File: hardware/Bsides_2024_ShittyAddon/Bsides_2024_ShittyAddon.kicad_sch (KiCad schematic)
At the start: 13 parts, among them J1 SWD, U1 PY32F002AA15M6TU

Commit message: feat(Hw): Update PCB
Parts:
- removed D4: Orange, LED_SMD:LED_0805_2012Metric, symbol Device:LED_Small
- removed R4: 330R, Resistor_SMD:R_0805_2012Metric, symbol Device:R_Small

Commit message: feat(Hw): Update PCB
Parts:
- removed J1: SWD, Footprints:PinHeader_1x04_P2.54mm_Vertical, symbol Connector:Conn_01x04_Pin
- added J2: Conn_02x03_Odd_Even, Footprints:B-2100N06P-B111_CKM, symbol Connector_Generic:Conn_02x03_Odd_Even
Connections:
- net +3.3V: now also J2.6 (Pin_6)
- net GND: now also J2.5 (Pin_5)
- net SWCLK: now also J2.2 (Pin_2)
- net SWDIO: now also J2.1 (Pin_1)
- no-connect marks 0 -> 2
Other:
- note added: "Shitty Add-on"

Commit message: Update route and schematic
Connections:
- net PA1: now also J2.3 (Pin_3); no longer D3.2 (A)
- net PA7: now also D3.2 (A); no longer D2.2 (A)
- net PF0: now also D2.2 (A)
- no-connect marks 2 -> 1
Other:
- moved on the sheet: D2, D3, J2, R2, R3

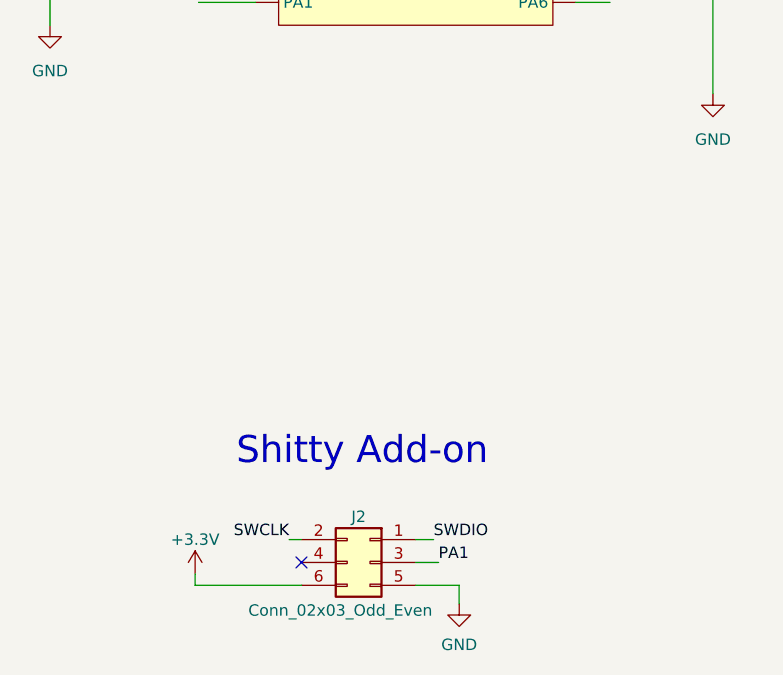
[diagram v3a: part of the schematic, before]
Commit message: feat(Hw): Update route
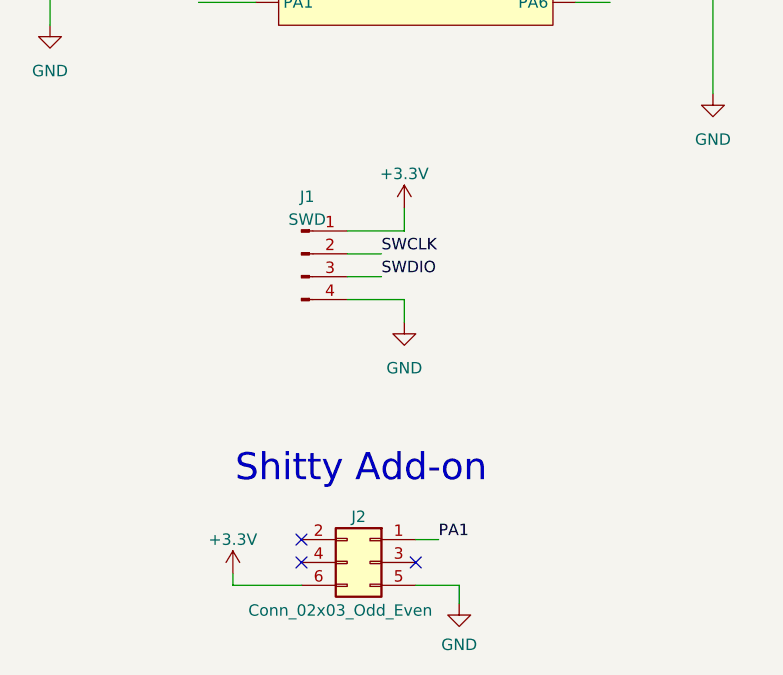
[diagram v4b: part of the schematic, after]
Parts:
- added J1: SWD, Footprints:PinHeader_1x04_P2.54mm_Vertical, symbol Connector:Conn_01x04_Pin
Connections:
- net +3.3V: now also J1.1 (Pin_1)
- net GND: now also J1.4 (Pin_4)
- net PA1: now also J2.1 (Pin_1); no longer J2.3 (Pin_3)
- net SWCLK: now also J1.2 (Pin_2); no longer J2.2 (Pin_2)
- net SWDIO: now also J1.3 (Pin_3); no longer J2.1 (Pin_1)
- no-connect marks 1 -> 3

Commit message: feat(Hw): Update BOM ShittyAddon
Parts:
- J1: now not fitted
- J2: LCSC# C706893 -> C124390
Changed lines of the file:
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@@
 			)
 		)
-		(property "LCSC#" "C706893"
+		(property "LCSC#" "C124390"
 			(at 55.88 109.22 0)
 			(effects
@@
 		(in_bom yes)
 		(on_board yes)
-		(dnp no)
+		(dnp yes)
 		(fields_autoplaced yes)
 		(property "Reference" "J1"
